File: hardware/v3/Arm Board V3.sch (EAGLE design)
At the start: 39 parts, among them CN1 1X4-BIG, IC1 L6208D, IC2 L6208D, IC3 L6208D, U1 MAX3468CSA

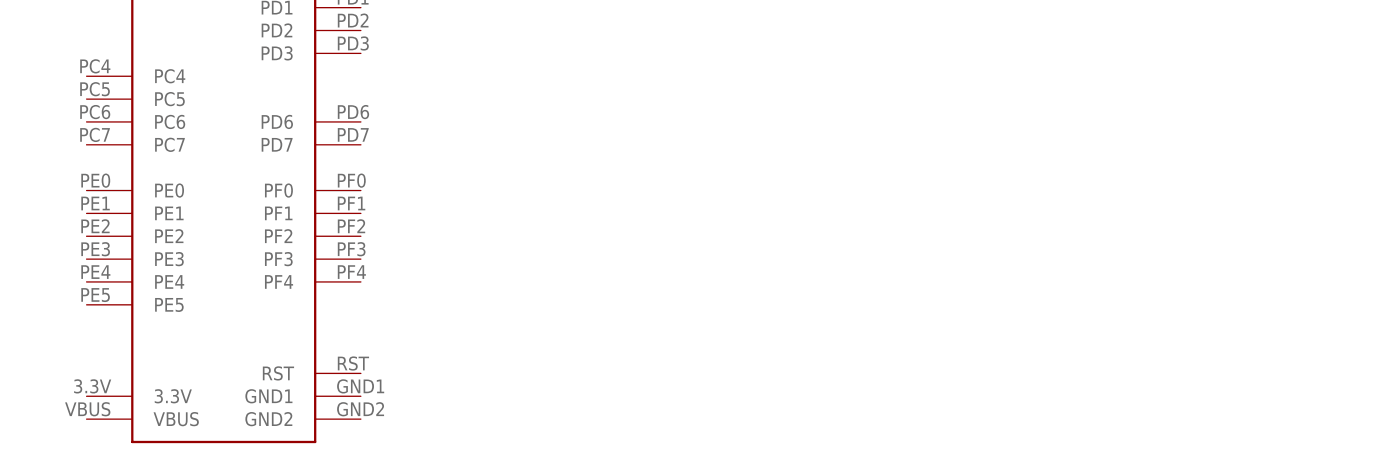
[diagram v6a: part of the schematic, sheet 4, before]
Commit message: Started routing and added RJ-45
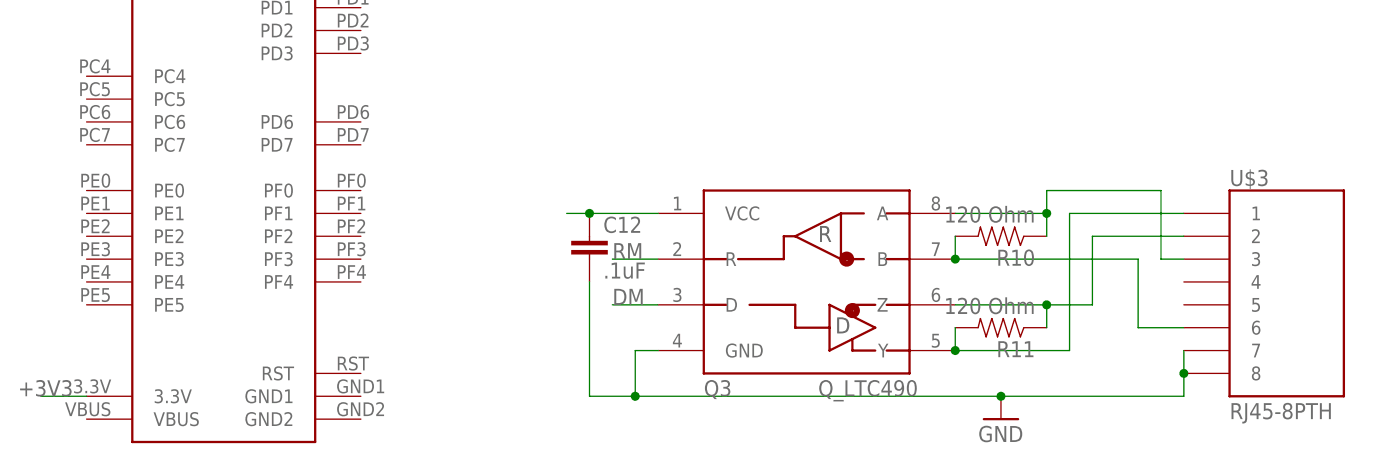
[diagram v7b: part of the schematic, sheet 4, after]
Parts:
- added C12: .1uF, SparkFun-Capacitors:CAPKIT
- added Q3: Q_LTC490, PCB0M1:Q_LTC490
- added R10, R11: 120 Ohm, SparkFun-Passives:RESISTORAXIAL-0.3
- added U$3: RJ45-8PTH, SparkFun-Connectors:RJ45-8PTH
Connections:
- new net +3V3: U$1.3.3V
- new net DM: Q3.D
- new net N$1: Q3.Z, R11.1, U$3.2
- new net N$2: Q3.B, R10.2, U$3.6
- new net N$3: Q3.A, R10.1, U$3.3
- new net N$5: Q3.Y, R11.2, U$3.1
- new net RM: Q3.R
- net +5V: now also C12.1, Q3.VCC
- net GND: now also C12.2, Q3.GND, U$3.7, U$3.8
- net OCD_A_1: no longer IC2.OCD_A
- net OCD_A_2: now also IC2.OCD_A

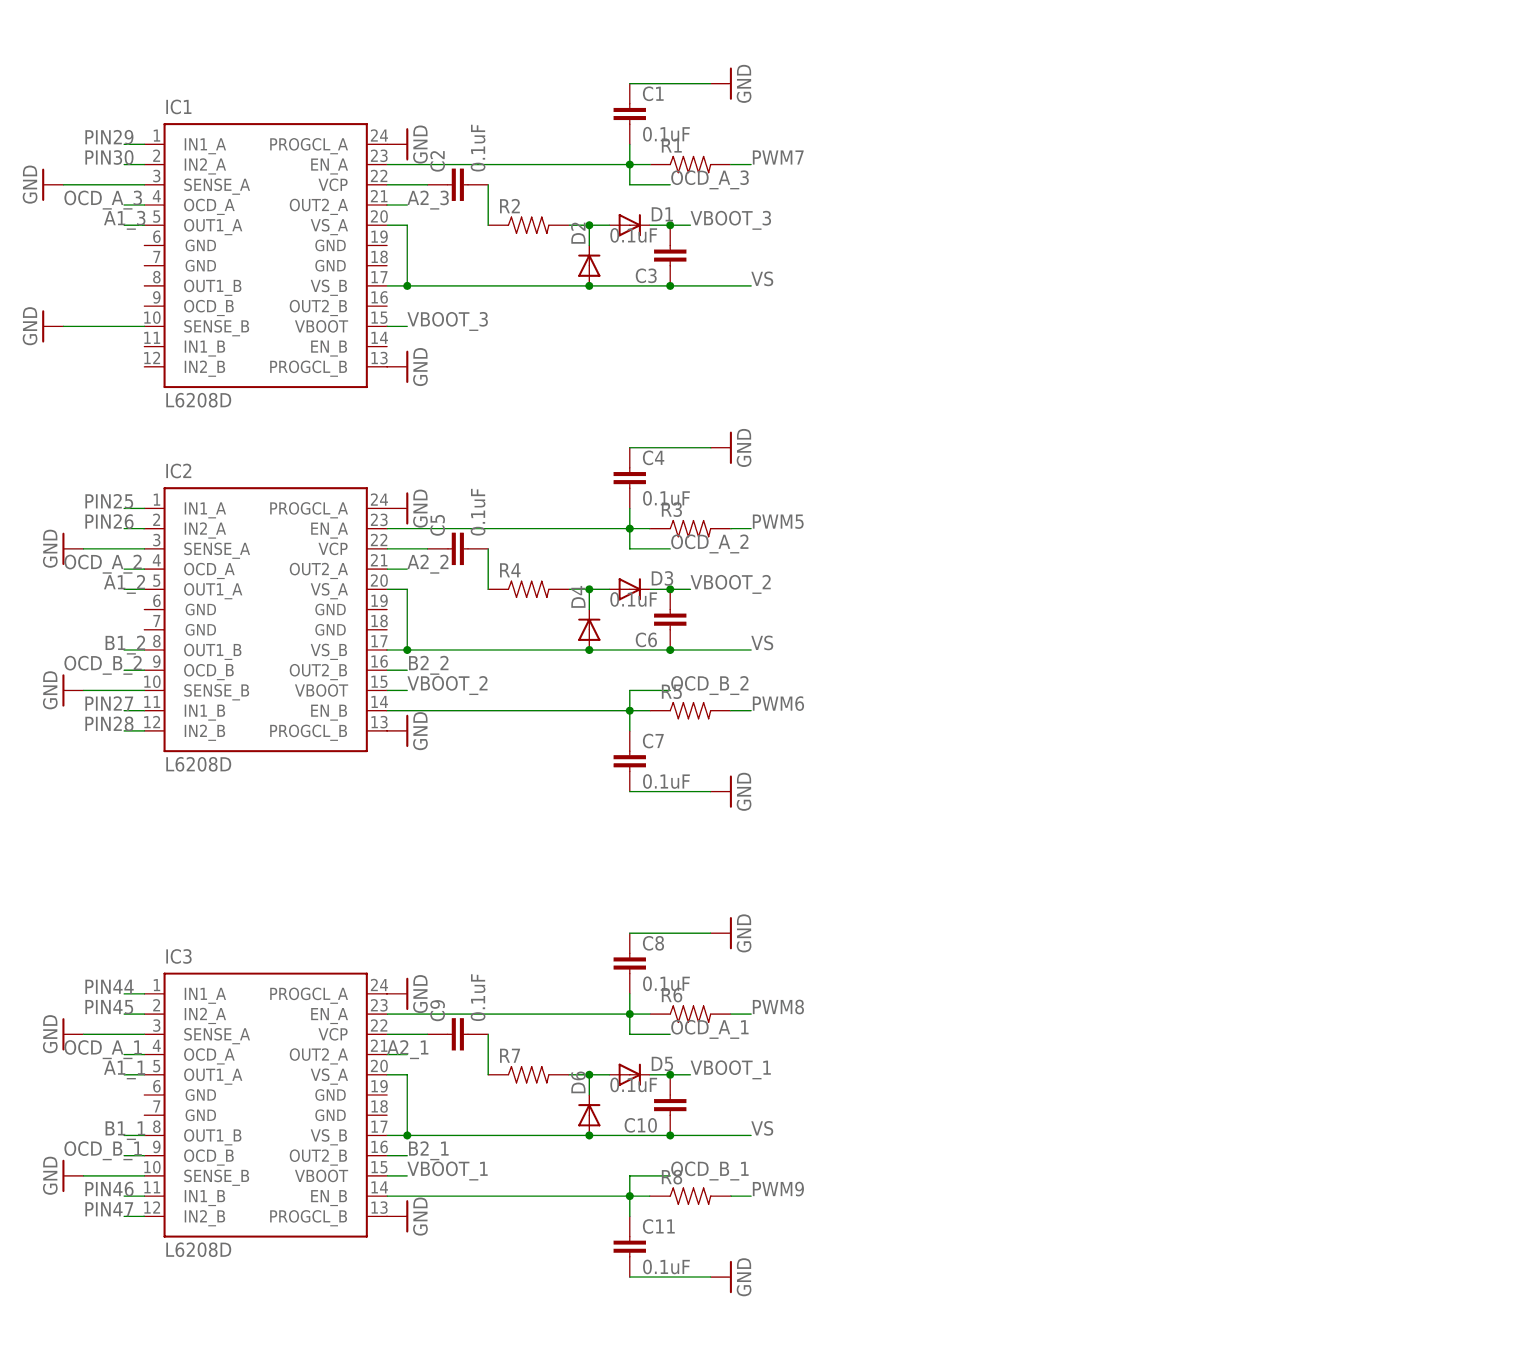
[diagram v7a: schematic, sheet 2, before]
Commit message: Started assigning serial pins and routing
Also added picture of TI Launchpad pinout (It will be fun when it comes
time to add encoders)
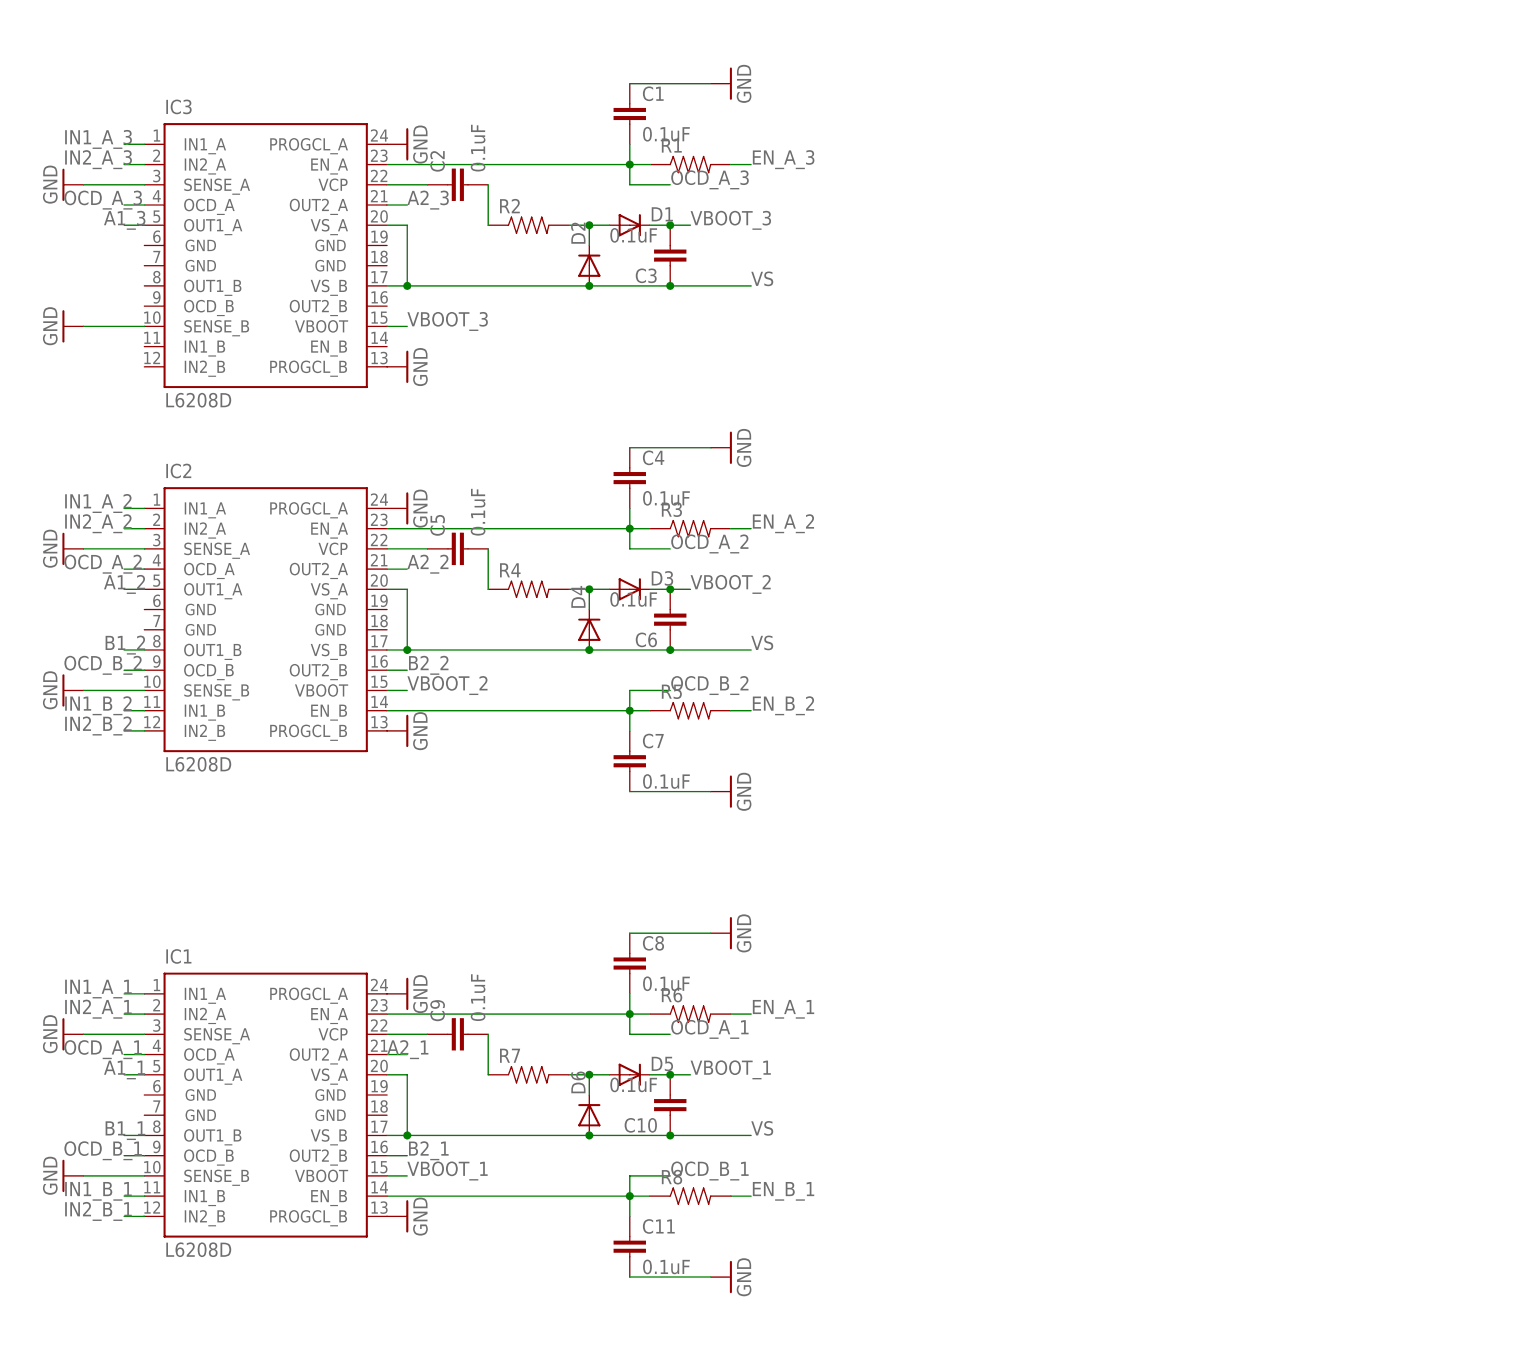
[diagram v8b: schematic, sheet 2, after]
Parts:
- added H1, H2, H3, H4: (no value), Lib_TH:H_MNTHOLE_#4
- R10, R11: device SparkFun-Passives:RESISTORAXIAL-0.3 -> SparkFun-Passives:RESISTOR0603-RES
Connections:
- net +12V renamed +18V
- net PIN25 renamed IN1_A_2
- net PIN26 renamed IN2_A_2
- net PIN27 renamed IN1_B_2
- net PIN28 renamed IN2_B_2
- net PIN29 renamed IN1_A_1
- net PIN30 renamed IN2_A_1
- net PIN44 renamed IN1_A_3
- net PIN45 renamed IN2_A_3
- net PWM5 renamed EN_A_2
- net PWM6 renamed EN_B_2
- net PWM7 renamed EN_A_3
- net PWM8 renamed EN_A_1
- net PWM9 renamed EN_B_1
- removed net +5V: C12.1, Q3.VCC, U$2.VDD, U1.VCC
- removed net DM: Q3.D
- removed net PIN23: U1.DE, U1.RE/
- removed net PIN46: IC3.IN1_B
- removed net PIN47: IC3.IN2_B
- removed net RM: Q3.R
- new net EN485: U$1.PB3, U1.DE, U1.RE/
- new net IN1_B_1: IC1.IN1_B
- new net IN2_B_1: IC1.IN2_B
- new net RESET: U$1.RST
- new net RXD3: U$1.PD6, U$2.DOUT
- new net TXD3: U$1.PD7, U$2.DIN
- new net XRESET: U$1.PF4, U$2.RESET
- net +3V3: now also C12.1, Q3.VCC, U$2.VDD, U1.VCC
- net A1_1: now also IC1.OUT1_A; no longer IC3.OUT1_A
- net A1_3: now also IC3.OUT1_A; no longer IC1.OUT1_A
- net A2_1: now also IC1.OUT2_A; no longer IC3.OUT2_A
- net A2_3: now also IC3.OUT2_A; no longer IC1.OUT2_A
- net B1_1: now also IC1.OUT1_B; no longer IC3.OUT1_B
- net B2_1: now also IC1.OUT2_B; no longer IC3.OUT2_B
- net GND: now also H1.1, H2.1, H3.1, H4.1, U$1.GND1, U$1.GND2
- net N$13: now also IC1.VCP; no longer IC3.VCP
- net N$19: now also IC3.VCP; no longer IC1.VCP
- net OCD_A_1: now also IC1.EN_A, IC1.OCD_A; no longer IC3.EN_A, IC3.OCD_A
- net OCD_A_3: now also IC3.EN_A, IC3.OCD_A; no longer IC1.EN_A, IC1.OCD_A
- net OCD_B_1: now also IC1.EN_B, IC1.OCD_B; no longer IC3.EN_B, IC3.OCD_B
- net RXD1: now also Q3.R, U$1.PC6; no longer U1.RO
- net RXD2: now also U$1.PC4, U1.RO; no longer U$2.DOUT
- net TXD1: now also Q3.D, U$1.PC7; no longer U1.DI
- net TXD2: now also U$1.PC5, U1.DI; no longer U$2.DIN
- net VBOOT_1: now also IC1.VBOOT; no longer IC3.VBOOT
- net VBOOT_3: now also IC3.VBOOT; no longer IC1.VBOOT
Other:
- moved on the sheet: IC1, IC3
